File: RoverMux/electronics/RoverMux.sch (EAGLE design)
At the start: 24 parts, among them J1 ISP, U1 TINY13, U2 MCP1824T, U3 74LS157D

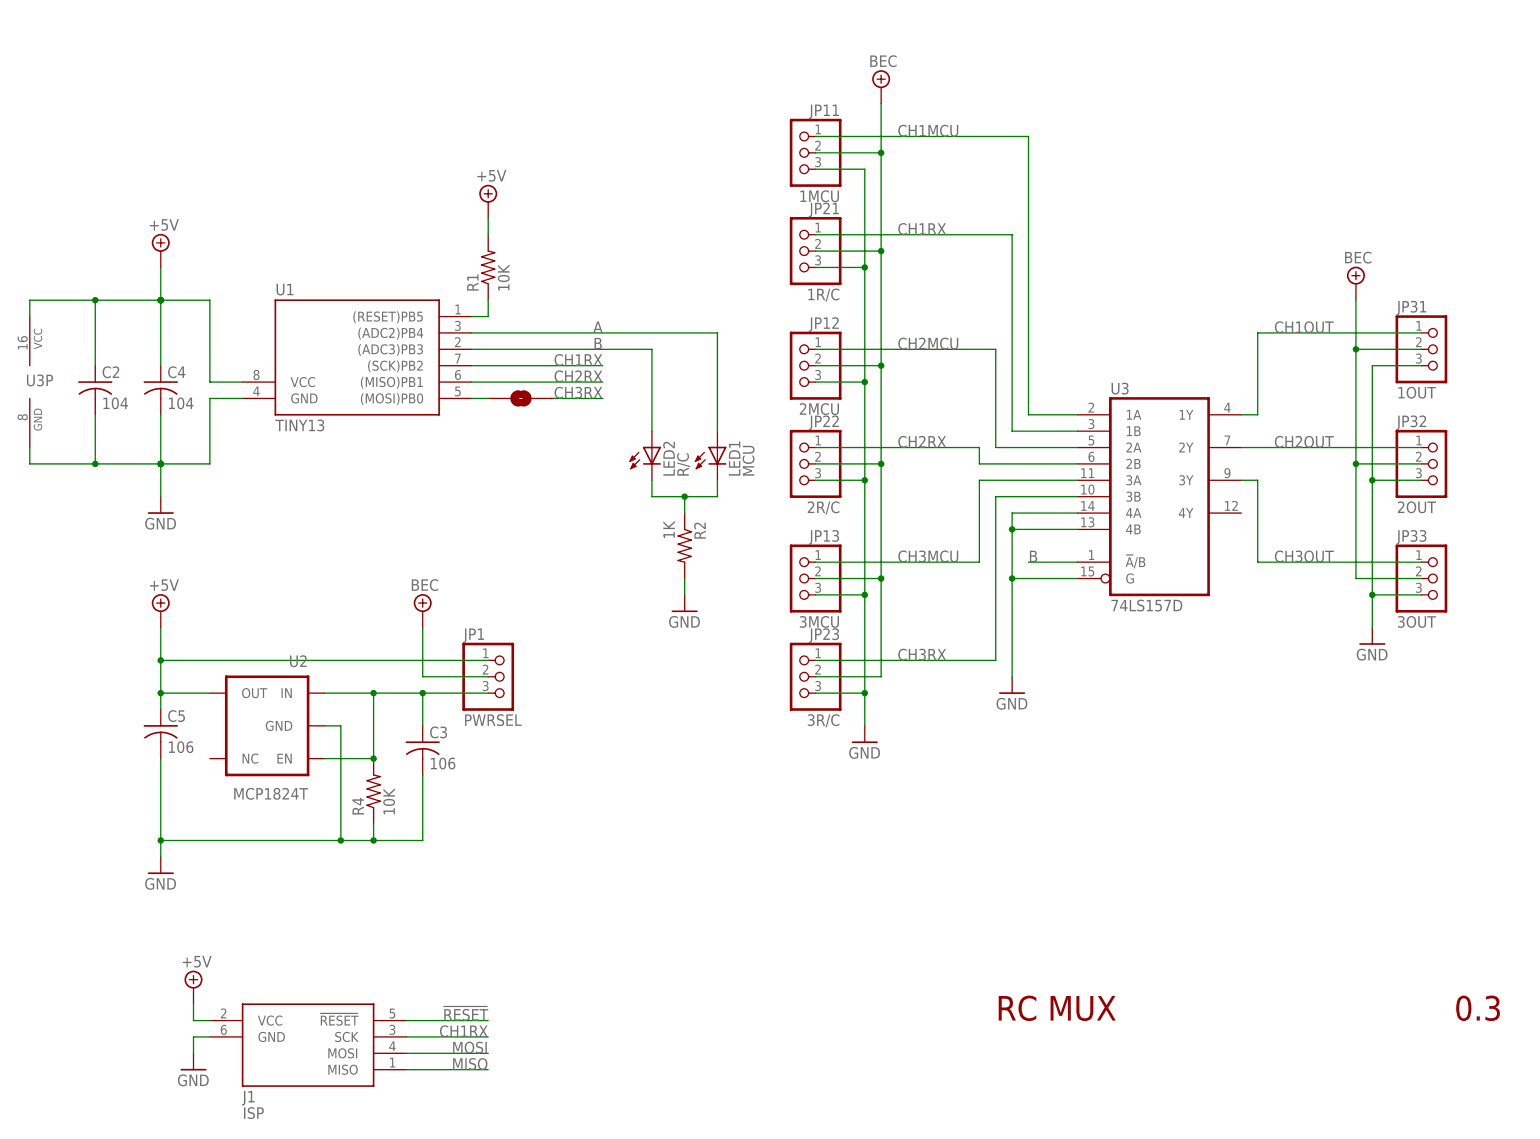
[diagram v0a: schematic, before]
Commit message: RoverMux electronics changes, minor software changes
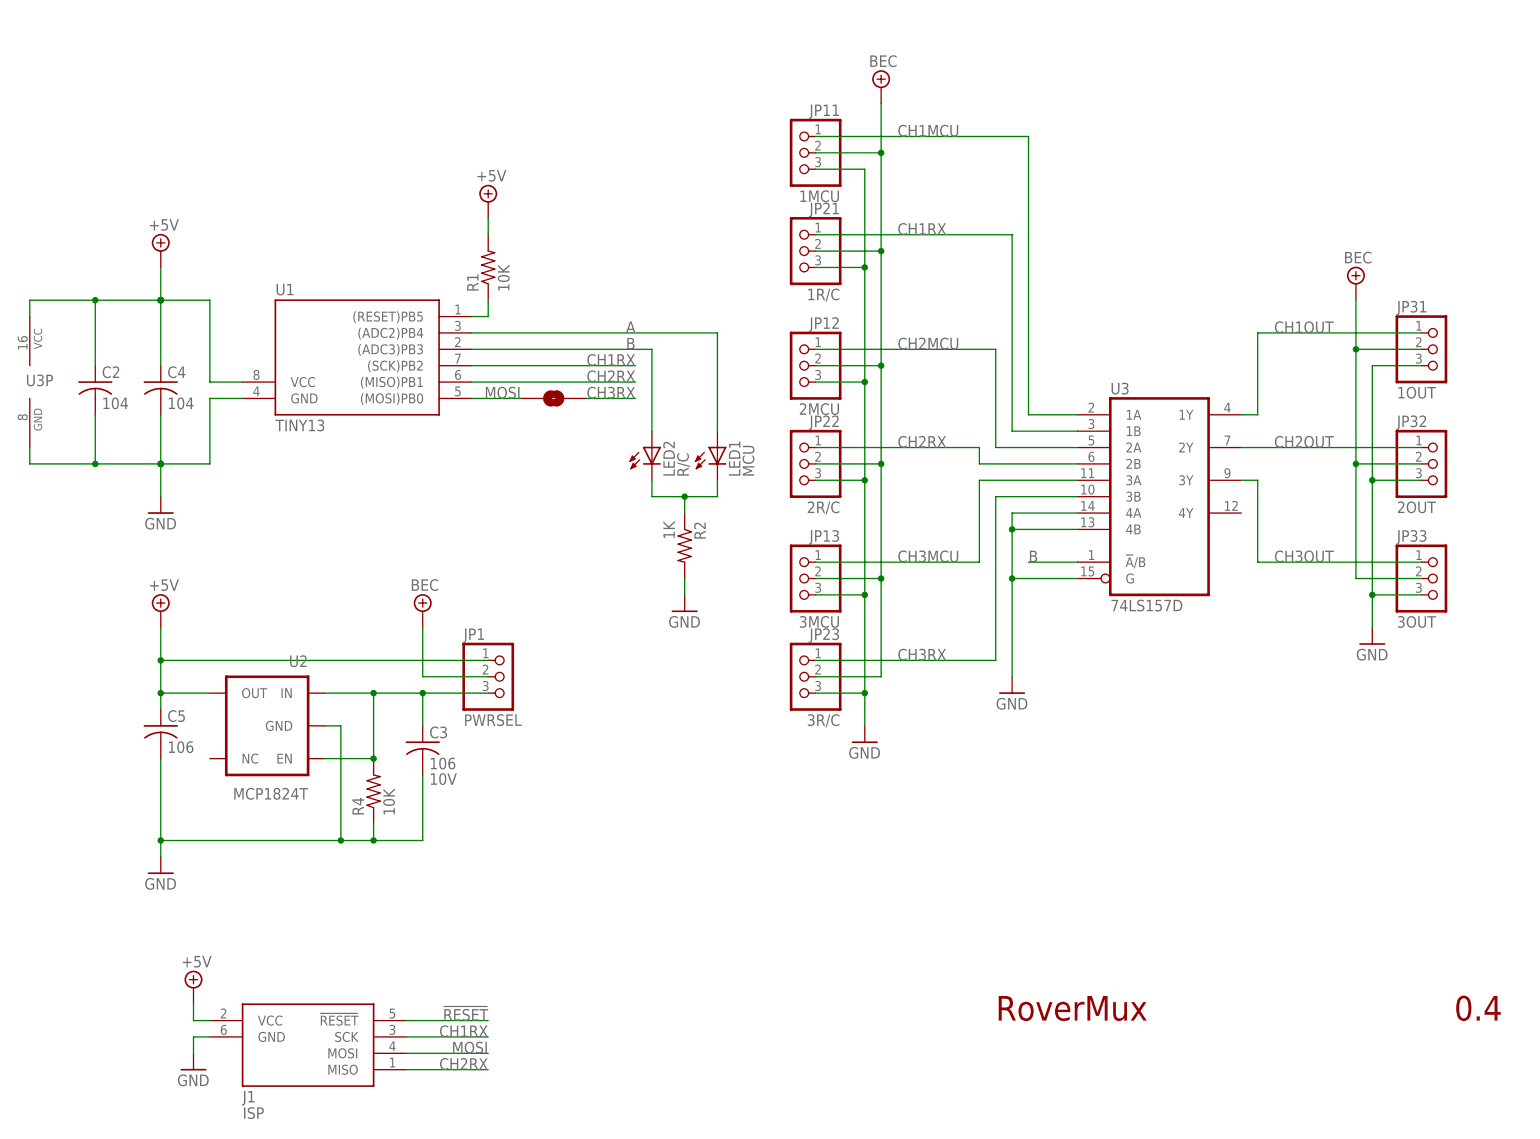
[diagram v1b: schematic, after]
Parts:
- C3: VOLTAGE (none) -> 10V
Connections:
- removed net MISO: J1.MISO
- net CH2RX: now also J1.MISO
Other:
- note added: "0.4"
- note added: "RoverMux"
- note removed: "0.3"
- note removed: "RC MUX"
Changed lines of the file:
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@@
 <part name="C3" library="rcl" deviceset="C-US" device="C0603" value="106">
 <attribute name="PARTNO" value="CL10A106MP8NNNC"/>
+<attribute name="VOLTAGE" value="10V"/>
 </part>
 <part name="U3" library="74xx-us" deviceset="74*157" device="D" technology="LS">
@@
 <sheet>
 <plain>
-<text x="162.56" y="22.86" size="3.81" layer="94">RC MUX</text>
-<text x="233.68" y="22.86" size="3.81" layer="94">0.3</text>
+<text x="162.56" y="22.86" size="3.81" layer="94">RoverMux</text>
+<text x="233.68" y="22.86" size="3.81" layer="94">0.4</text>
 </plain>
 <instances>
@@
 <instance part="C3" gate="G$1" x="73.66" y="66.04">
 <attribute name="PARTNO" x="73.66" y="66.04" size="1.778" layer="96" rot="R90" display="off"/>
+<attribute name="VOLTAGE" x="74.676" y="59.436" size="1.778" layer="96"/>
 </instance>
 <instance part="U3" gate="A" x="187.96" y="104.14">
@@
 <attribute name="PARTNO" x="66.04" y="58.42" size="1.778" layer="96" display="off"/>
 </instance>
-<instance part="SJ1" gate="1" x="88.9" y="119.38" smashed="yes"/>
+<instance part="SJ1" gate="1" x="93.98" y="119.38" smashed="yes"/>
 <instance part="J1" gate="A" x="55.88" y="15.24"/>
 <instance part="SUPPLY6" gate="+5V" x="38.1" y="27.94"/>
@@
 <segment>
 <pinref part="U1" gate="G$1" pin="(SCK)PB2"/>
-<wire x1="81.28" y1="124.46" x2="101.6" y2="124.46" width="0.1524" layer="91"/>
-<label x="101.6" y="124.46" size="1.778" layer="95" rot="MR0"/>
+<wire x1="81.28" y1="124.46" x2="106.68" y2="124.46" width="0.1524" layer="91"/>
+<label x="106.68" y="124.46" size="1.778" layer="95" rot="MR0"/>
 </segment>
 <segment>
@@
 <segment>
 <pinref part="U1" gate="G$1" pin="(MISO)PB1"/>
-<wire x1="81.28" y1="121.92" x2="101.6" y2="121.92" width="0.1524" layer="91"/>
-<label x="101.6" y="121.92" size="1.778" layer="95" rot="MR0"/>
+<wire x1="81.28" y1="121.92" x2="106.68" y2="121.92" width="0.1524" layer="91"/>
+<label x="106.68" y="121.92" size="1.778" layer="95" rot="MR0"/>
+</segment>
+<segment>
+<pinref part="J1" gate="A" pin="MISO"/>
+<wire x1="71.12" y1="15.24" x2="83.82" y2="15.24" width="0.1524" layer="91"/>
+<label x="83.82" y="15.24" size="1.778" layer="95" rot="MR0"/>
 </segment>
 </net>
@@
 </segment>
 <segment>
-<label x="101.6" y="119.38" size="1.778" layer="95" rot="MR0"/>
+<label x="106.68" y="119.38" size="1.778" layer="95" rot="MR0"/>
 <pinref part="SJ1" gate="1" pin="2"/>
-<wire x1="93.98" y1="119.38" x2="101.6" y2="119.38" width="0.1524" layer="91"/>
+<wire x1="99.06" y1="119.38" x2="106.68" y2="119.38" width="0.1524" layer="91"/>
 </segment>
 </net>
@@
 <pinref part="U1" gate="G$1" pin="(ADC3)PB3"/>
 <wire x1="109.22" y1="127" x2="81.28" y2="127" width="0.1524" layer="91"/>
-<label x="101.6" y="127" size="1.778" layer="95" rot="MR0"/>
+<label x="106.68" y="127" size="1.778" layer="95" rot="MR0"/>
 </segment>
 </net>
@@
 <pinref part="U1" gate="G$1" pin="(MOSI)PB0"/>
 <pinref part="SJ1" gate="1" pin="1"/>
-<wire x1="83.82" y1="119.38" x2="81.28" y2="119.38" width="0.1524" layer="91"/>
+<wire x1="88.9" y1="119.38" x2="81.28" y2="119.38" width="0.1524" layer="91"/>
+<label x="88.9" y="119.38" size="1.778" layer="95" rot="MR0"/>
 </segment>
 <segment>
@@
 <pinref part="U1" gate="G$1" pin="(ADC2)PB4"/>
 <wire x1="119.38" y1="129.54" x2="81.28" y2="129.54" width="0.1524" layer="91"/>
-<label x="101.6" y="129.54" size="1.778" layer="95" rot="MR0"/>
+<label x="106.68" y="129.54" size="1.778" layer="95" rot="MR0"/>
 </segment>
 </net>
@@
 </segment>
 </net>
-<net name="MISO" class="0">
-<segment>
-<pinref part="J1" gate="A" pin="MISO"/>
-<wire x1="71.12" y1="15.24" x2="83.82" y2="15.24" width="0.1524" layer="91"/>
-<label x="83.82" y="15.24" size="1.778" layer="95" rot="MR0"/>
-</segment>
-</net>

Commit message: Revised 8SOIC footprint, replaced 5V regulator and selector with 3.3V regulator to simplify. Moved devices around, simplified routing to pin headers. Placed missing ISP trace. Revised schematic layout.
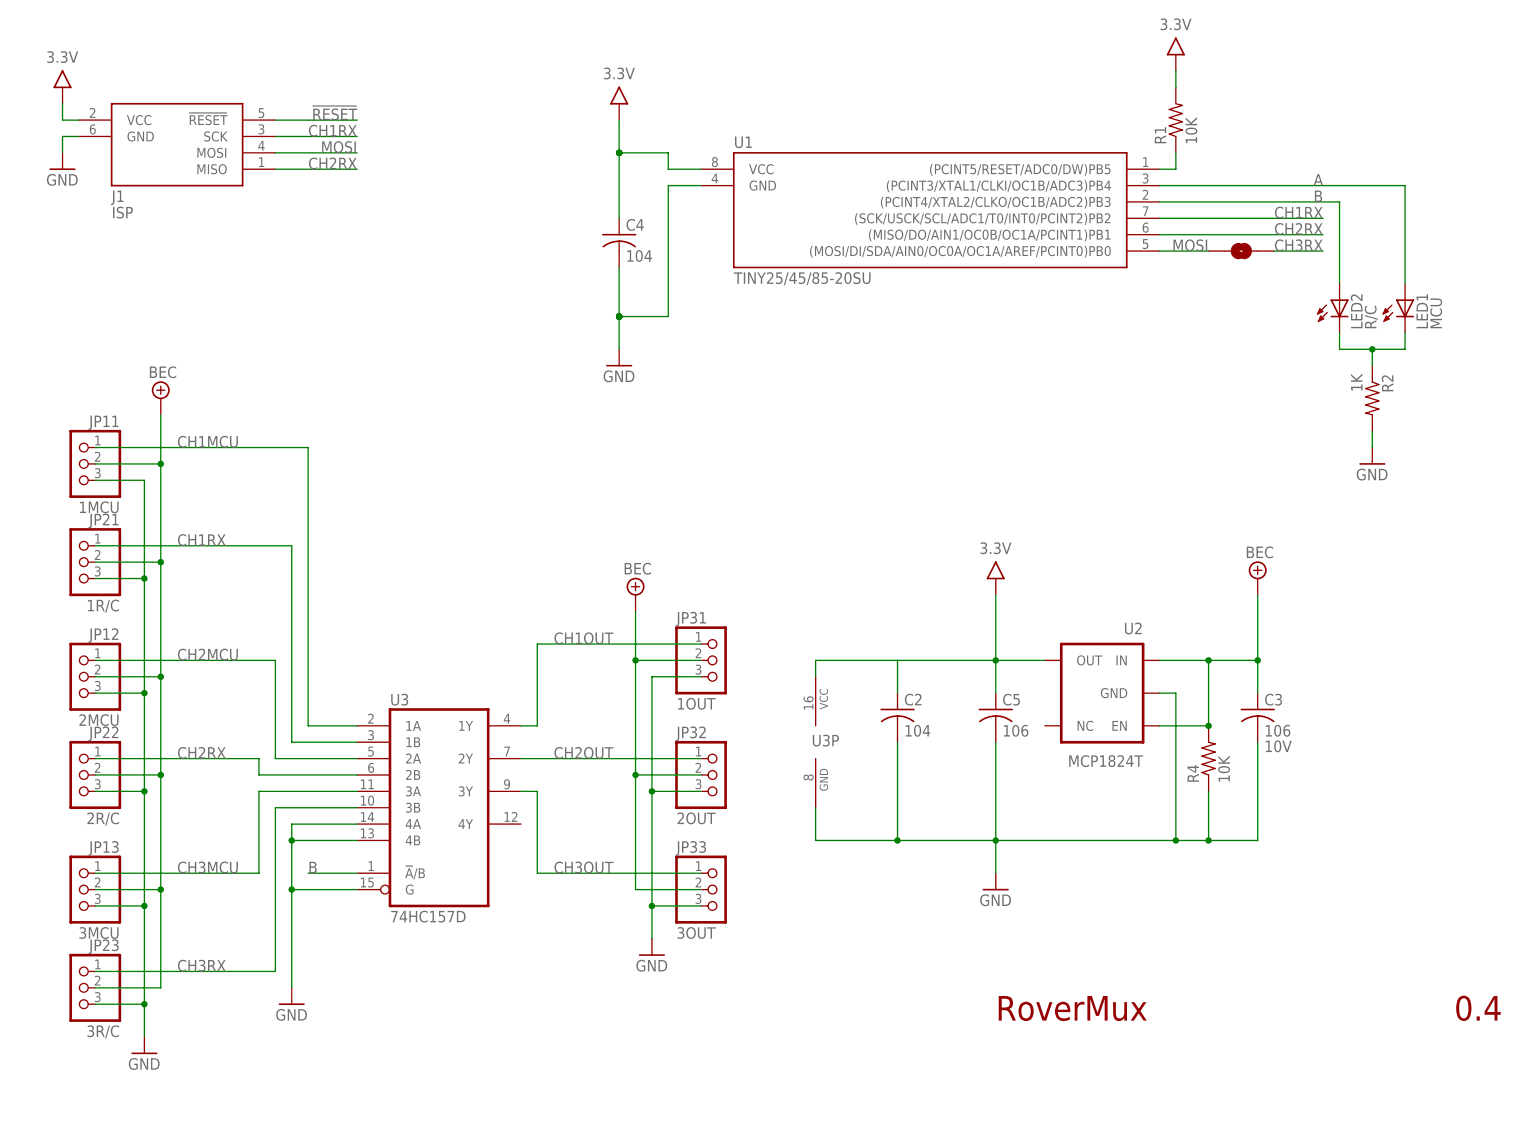
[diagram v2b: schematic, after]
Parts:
- removed JP1: PWRSEL, pinhead-2:PINHD-1X03_2.00
- U1: value TINY13 -> TINY25/45/85-20SU; device avr-7:TINY138S2 -> bt_avr:TINY25/45/85-20SU; PARTNO ATTINY13A-SSH -> (none)
- U3: value 74LS157D -> 74HC157D
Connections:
- removed net +5V: C2.1, C4.1, C5.1, J1.VCC, JP1.1, R1.2, U1.VCC, U2.OUT, U3P.VCC
- removed net +7V: JP1.2, JP11.2, JP12.2, JP13.2, JP21.2, JP22.2, JP23.2, JP31.2, JP32.2, JP33.2
- removed net REGIN: C3.1, JP1.3, R4.2, U2.EN, U2.IN
- new net 3.3V: C2.1, C4.1, C5.1, J1.VCC, R1.2, U1.VCC, U2.OUT, U3P.VCC
- new net BEC: C3.1, JP11.2, JP12.2, JP13.2, JP21.2, JP22.2, JP23.2, JP31.2, JP32.2, JP33.2, R4.2, U2.EN, U2.IN
- net !RESET: now also U1.(PCINT5/RESET/ADC0/DW)PB5; no longer U1.(RESET)PB5
- net A: now also U1.(PCINT3/XTAL1/CLKI/OC1B/ADC3)PB4; no longer U1.(ADC2)PB4
- net B: now also U1.(PCINT4/XTAL2/CLKO/OC1B/ADC2)PB3; no longer U1.(ADC3)PB3
- net CH1RX: now also U1.(SCK/USCK/SCL/ADC1/T0/INT0/PCINT2)PB2; no longer U1.(SCK)PB2
- net CH2RX: now also U1.(MISO/DO/AIN1/OC0B/OC1A/PCINT1)PB1; no longer U1.(MISO)PB1
- net MOSI: now also U1.(MOSI/DI/SDA/AIN0/OC0A/OC1A/AREF/PCINT0)PB0; no longer U1.(MOSI)PB0
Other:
- moved on the sheet: C2, C3, C4, C5, J1, JP11, JP12, JP13, JP21, JP22, JP23, JP31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
